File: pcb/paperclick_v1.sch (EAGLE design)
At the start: 83 parts, among them J1 SMT_JUMPER_2_NC_PASTE, J2 SMT_JUMPER_2_NC_PASTE, J3 SMT_JUMPER_2_NC_PASTE, P1 SMD-R1, P10 SMD-R1, P11 SMD-R1, P12 SMD-R1, P13 SMD-R1, P14 SMD-R1, P15 SMD-R1, P16 SMD-R1, P17 SMD-R1, P2 SMD-R1, P3 SMD-R1, P4 SMD-R1, P5 SMD-R1, P6 SMD-R1, P7 SMD-R1, P8 SMD-R1, P9 SMD-R1, Q1 NTNUS3171PZ, U1 WS4518D, U2 MIC5504, U3 ANT016008LCS2442MA2, U4 THD0515-30CL-SN, X1 XTAL_2016

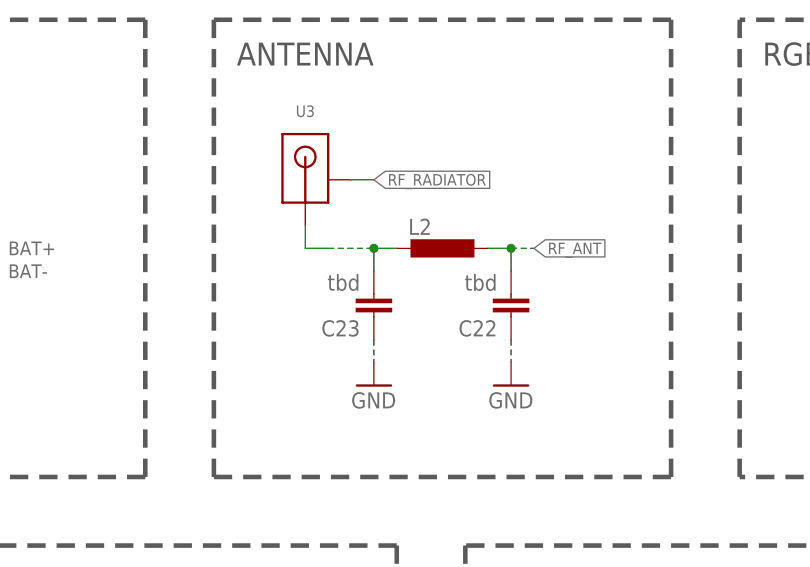
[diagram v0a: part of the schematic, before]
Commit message: updated schematics with correct values for the matching network
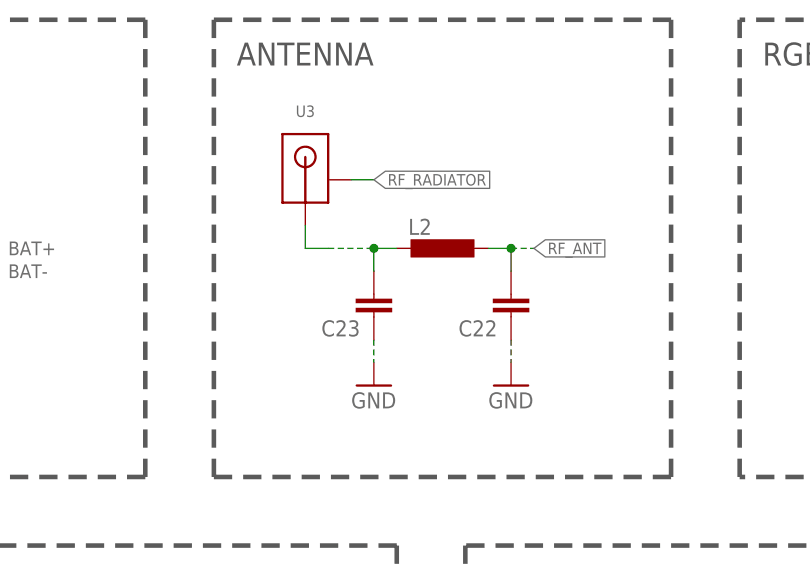
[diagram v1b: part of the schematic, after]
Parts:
- C22, C23: value tbd -> (none)
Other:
- note added: "1.8nH"
- note added: "7.3nH"
- note added: "L!!"
- note added: "dnm"
- note removed: "exchange with APA104 or else"
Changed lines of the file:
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@@
 <part name="+VBAT5" library="iml_elc" deviceset="+VBAT" device=""/>
 <part name="GND1" library="supply1" library_urn="urn:adsk.eagle:library:371" deviceset="GND" device=""/>
-<part name="C23" library="moekoe_rcl" library_urn="urn:adsk.eagle:library:34187148" deviceset="C0201" device="" package3d_urn="urn:adsk.eagle:package:34200839/2" value="tbd"/>
-<part name="C22" library="moekoe_rcl" library_urn="urn:adsk.eagle:library:34187148" deviceset="C0201" device="" package3d_urn="urn:adsk.eagle:package:34200839/2" value="tbd"/>
+<part name="C23" library="moekoe_rcl" library_urn="urn:adsk.eagle:library:34187148" deviceset="C0201" device="" package3d_urn="urn:adsk.eagle:package:34200839/2"/>
+<part name="C22" library="moekoe_rcl" library_urn="urn:adsk.eagle:library:34187148" deviceset="C0201" device="" package3d_urn="urn:adsk.eagle:package:34200839/2"/>
 <part name="L2" library="moekoe_rcl" library_urn="urn:adsk.eagle:library:34187148" deviceset="L0201" device="" package3d_urn="urn:adsk.eagle:package:34200841/2"/>
 <part name="U1" library="moekoe_ics" library_urn="urn:adsk.eagle:library:34187141" deviceset="WS4518D" device="" package3d_urn="urn:adsk.eagle:package:32881971/1"/>
@@
 <plain>
 <text x="483.87" y="48.26" size="2.54" layer="94">Moritz König</text>
-<text x="401.32" y="269.24" size="1.27" layer="98" font="vector">exchange with APA104 or else</text>
 <wire x1="345.44" y1="218.44" x2="345.44" y2="142.24" width="0.508" layer="97" style="longdash"/>
 <wire x1="345.44" y1="142.24" x2="419.1" y2="142.24" width="0.508" layer="97" style="longdash"/>
@@
 <text x="429.26" y="101.6" size="2.54" layer="97" font="vector" ratio="20">USER BUTTON</text>
 <text x="373.38" y="180.34" size="1.27" layer="98">250k</text>
+<text x="342.9" y="254" size="1.27" layer="98">7.3nH</text>
+<text x="353.06" y="243.84" size="1.27" layer="98">1.8nH</text>
+<text x="353.06" y="246.38" size="1.27" layer="98">L!!</text>
+<text x="330.2" y="246.38" size="1.27" layer="98">dnm</text>
 </plain>
 <instances>
